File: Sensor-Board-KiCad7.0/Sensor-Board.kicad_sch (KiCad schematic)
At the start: 73 parts, among them J2 B04B-XASK-1, U1 OPA396DCKT, U10 BME680, U14 OPA396DCKT, U19 MMBFJ177LT1, U2 OPA396DCKT, U20 MMBFJ177LT1, U21 OPA396DCKT, U22 OPA396DCKT, U25 NAU7802SGI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

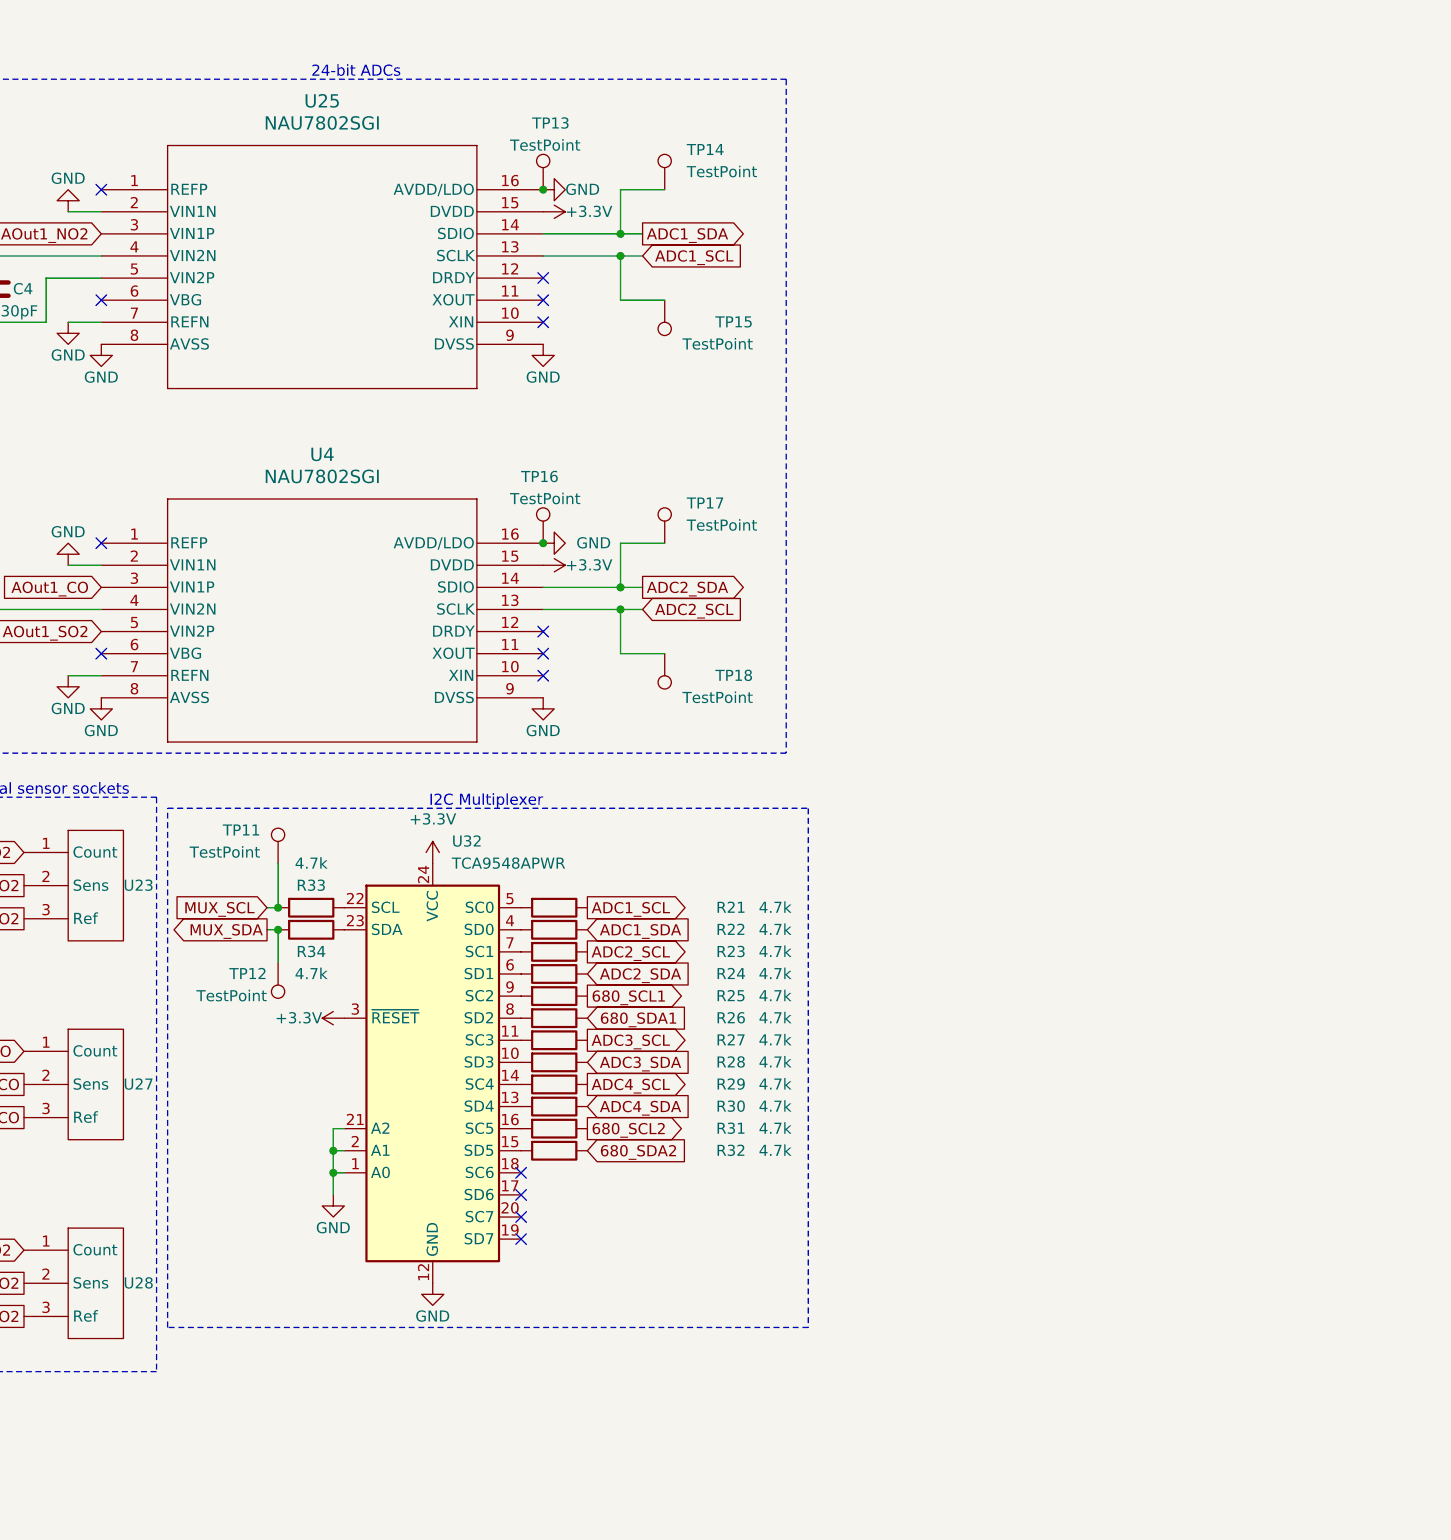
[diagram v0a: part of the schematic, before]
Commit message: Added PU resistors to multiplexer
Added pull-up resistor to RESET as well as decoupling capacitors to digital multiplexer. Fixed routing intersection errors.
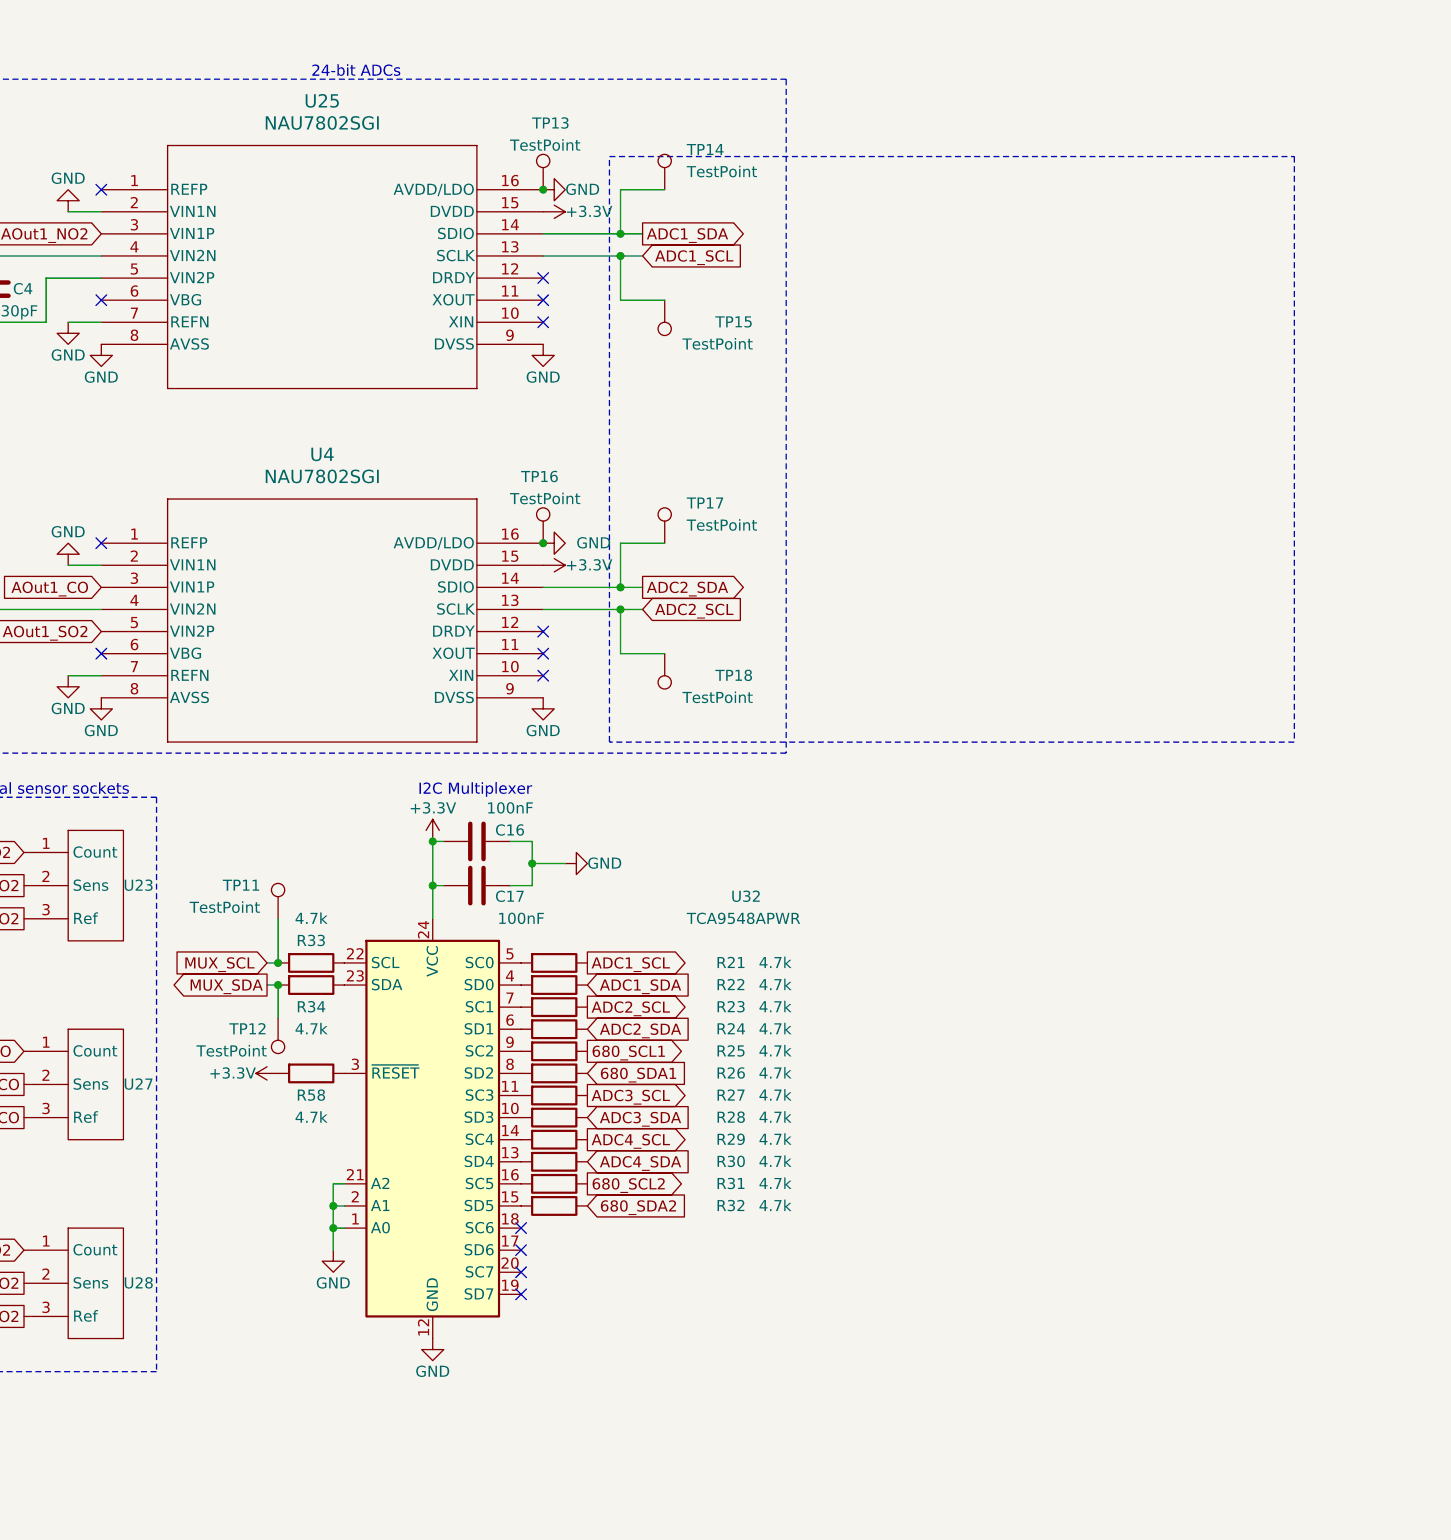
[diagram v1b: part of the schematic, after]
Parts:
- added C16, C17: 100nF, Capacitor_SMD:C_0603_1608Metric, symbol Device:C
- added R58: 4.7k, Resistor_SMD:R_0603_1608Metric, symbol Device:R
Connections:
- net +3.3V: now also C16.2, C17.2, R58.2; no longer U32.3 (~{RESET})
- net GND: now also C16.1, C17.1
- new net: R58.1, U32.3 (~{RESET})
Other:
- moved on the sheet: R21, R22, R23, R24, R25, R26, R27, R28, R29, R30, R31, R32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

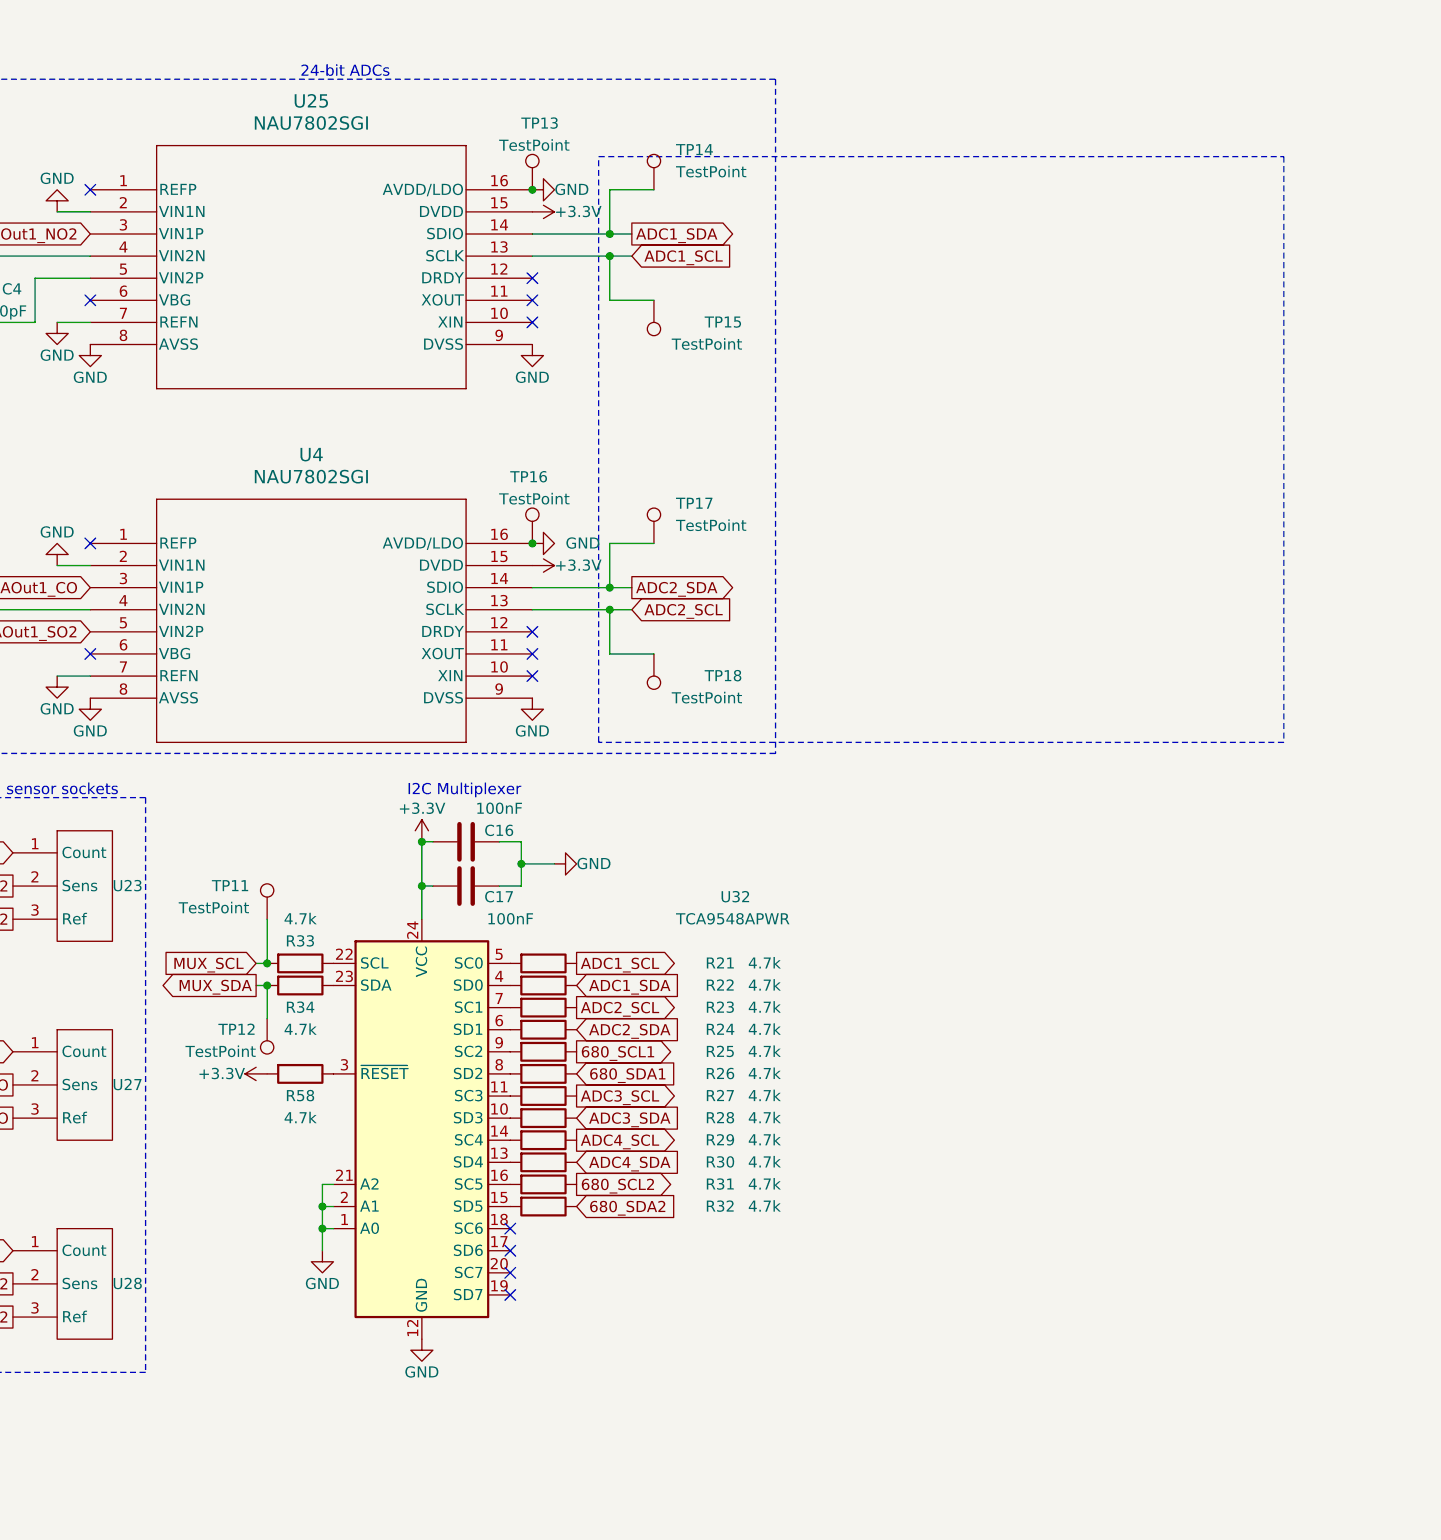
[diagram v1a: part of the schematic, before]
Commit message: Added board name
Added board name and increased Echem socket diameter to 1.46mm to account for tolerances.
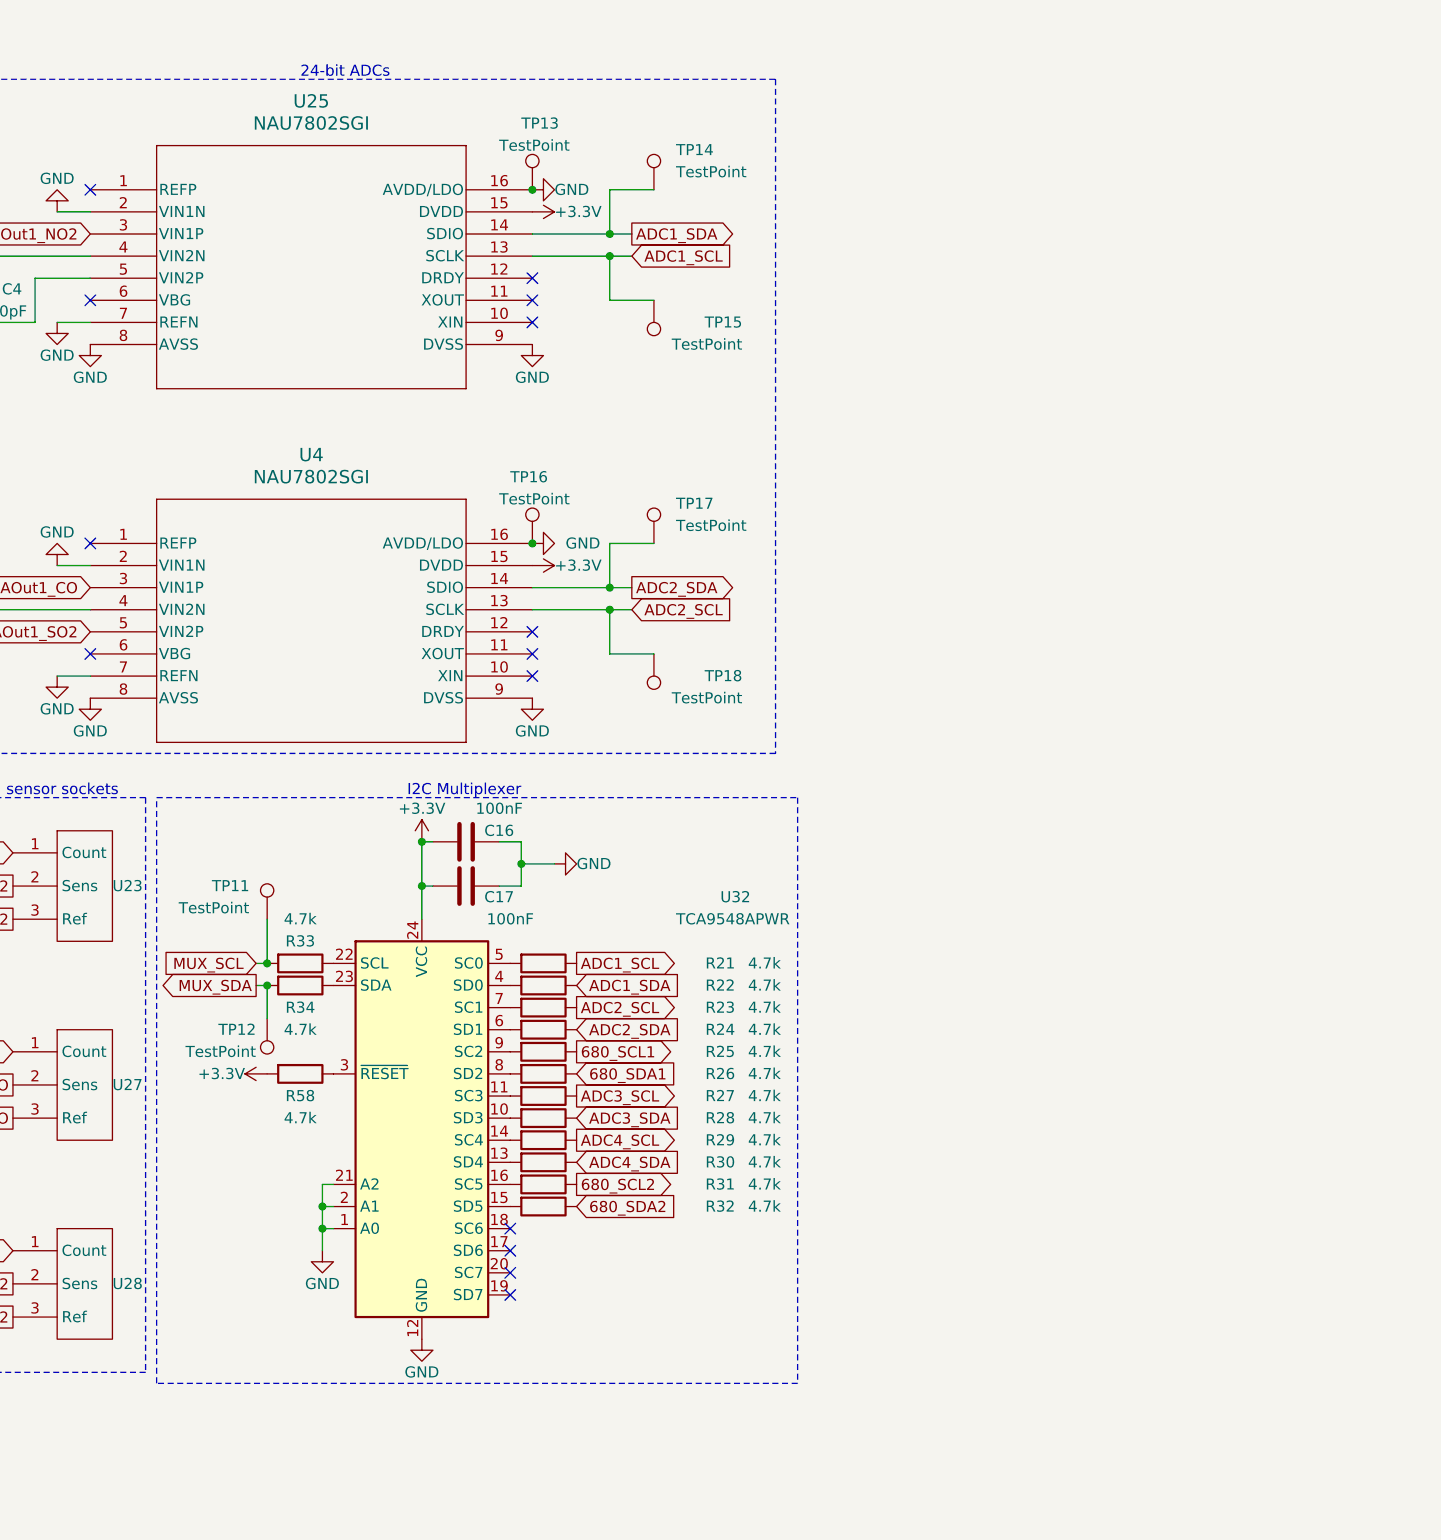
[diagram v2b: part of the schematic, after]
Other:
- title: Payload Sensor Board -> Gas Recognition Unit
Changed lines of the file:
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@@
   (paper "A4")
   (title_block
-    (title "Payload Sensor Board")
+    (title "Gas Recognition Unit")
     (date "2024-03-23")
     (rev "1.0")
@@
     (fill (type none))
   )
-  (rectangle (start 260.35 24.13) (end 339.09 91.44)
+  (rectangle (start 209.55 97.79) (end 283.21 165.1)
     (stroke (width 0) (type dash))
     (fill (type none))

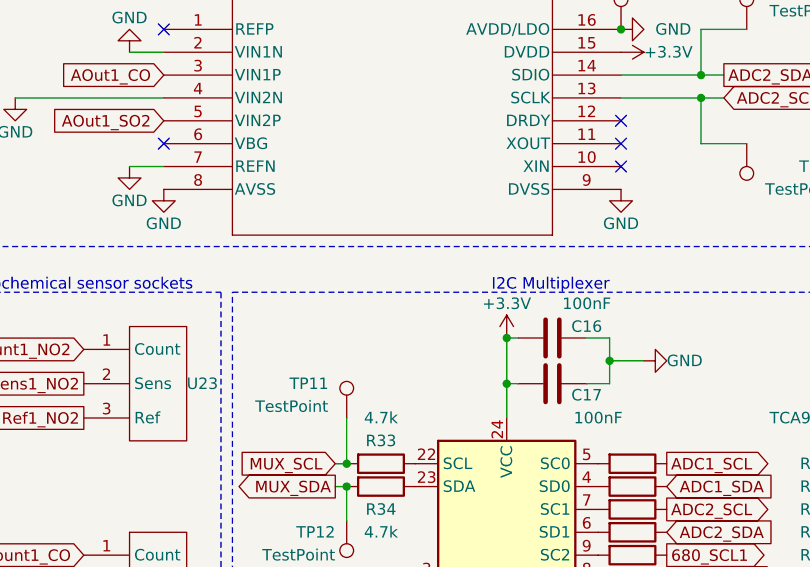
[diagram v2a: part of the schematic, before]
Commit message: Added gru logo and generated BOMs
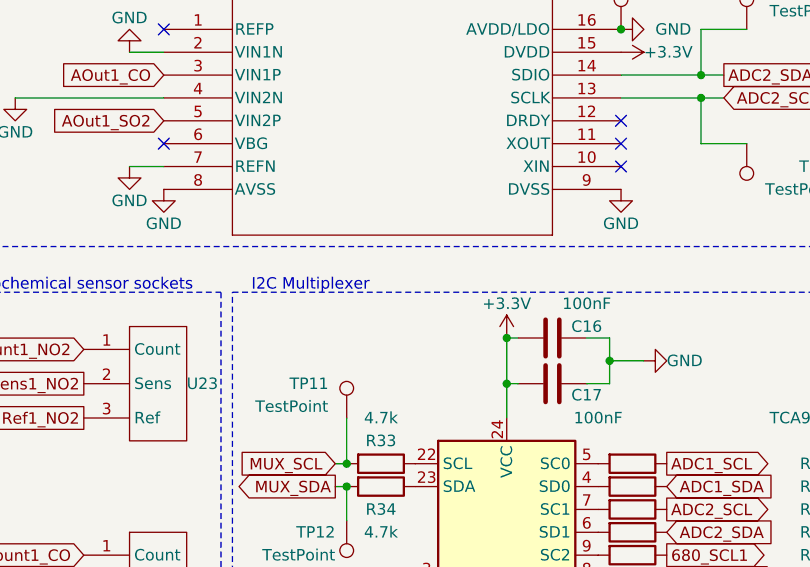
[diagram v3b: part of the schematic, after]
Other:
- title: Gas Recognition Unit -> Payload Sensor Board
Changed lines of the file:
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@@
   (paper "A4")
   (title_block
-    (title "Gas Recognition Unit")
+    (title "Payload Sensor Board")
     (date "2024-03-23")
     (rev "1.0")
@@
     (effects (font (size 1.27 1.27)) (justify left bottom))
   )
-  (text "I2C Multiplexer" (at 251.46 97.79 0)
+  (text "I2C Multiplexer" (at 224.79 97.79 0)
     (effects (font (size 1.27 1.27)) (justify right bottom))
   )
